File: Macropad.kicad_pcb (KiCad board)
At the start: 2 copper layers, 62 x 83 mm, 21 parts, among them SW1 SW_Push, SW10 RotaryEncoder_Switch, SW2 SW_Push, SW3 SW_Push, SW4 SW_Push, SW5 SW_Push, SW6 SW_Push, SW7 SW_Push, SW8 SW_Push, SW9 SW_Push, U1 MOUDLE-SEEEDUINO-XIAO, U2 OLED_0.91_128x32

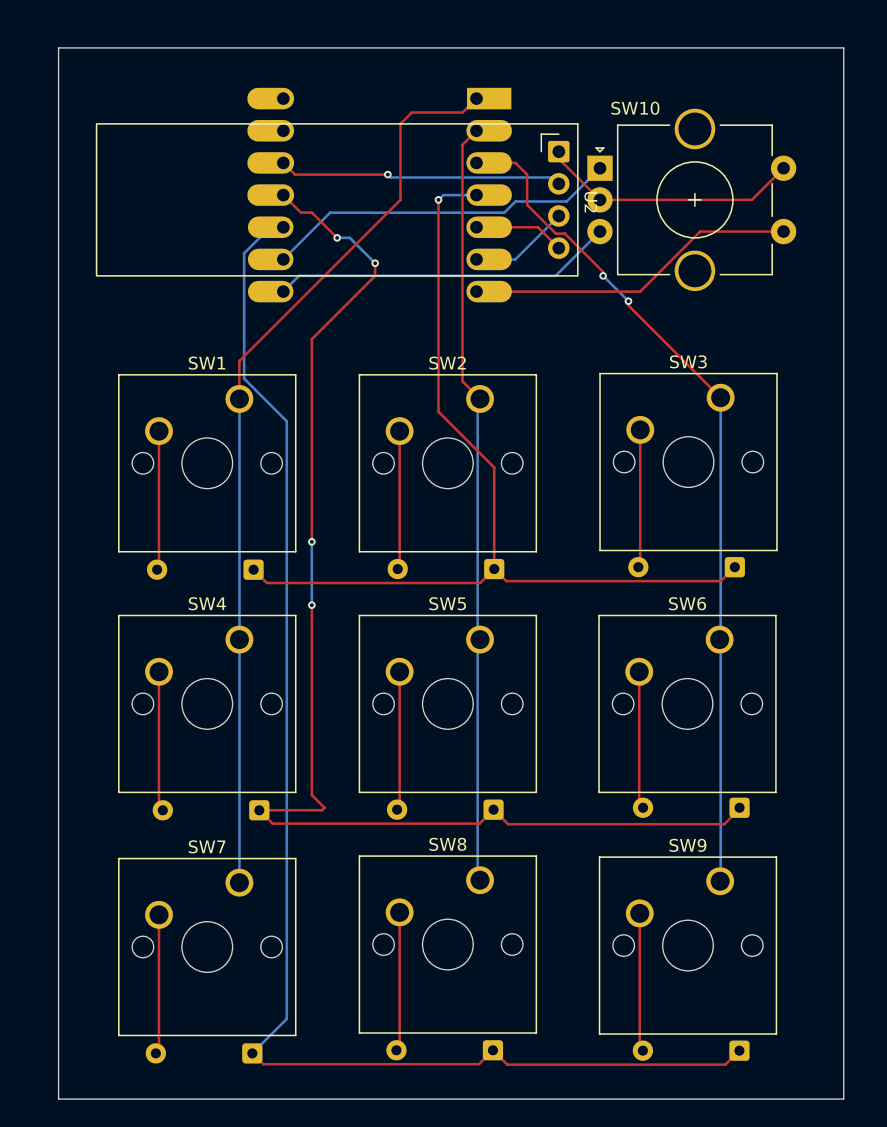
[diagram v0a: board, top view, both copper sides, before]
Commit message: noch löcher hinzugefügt
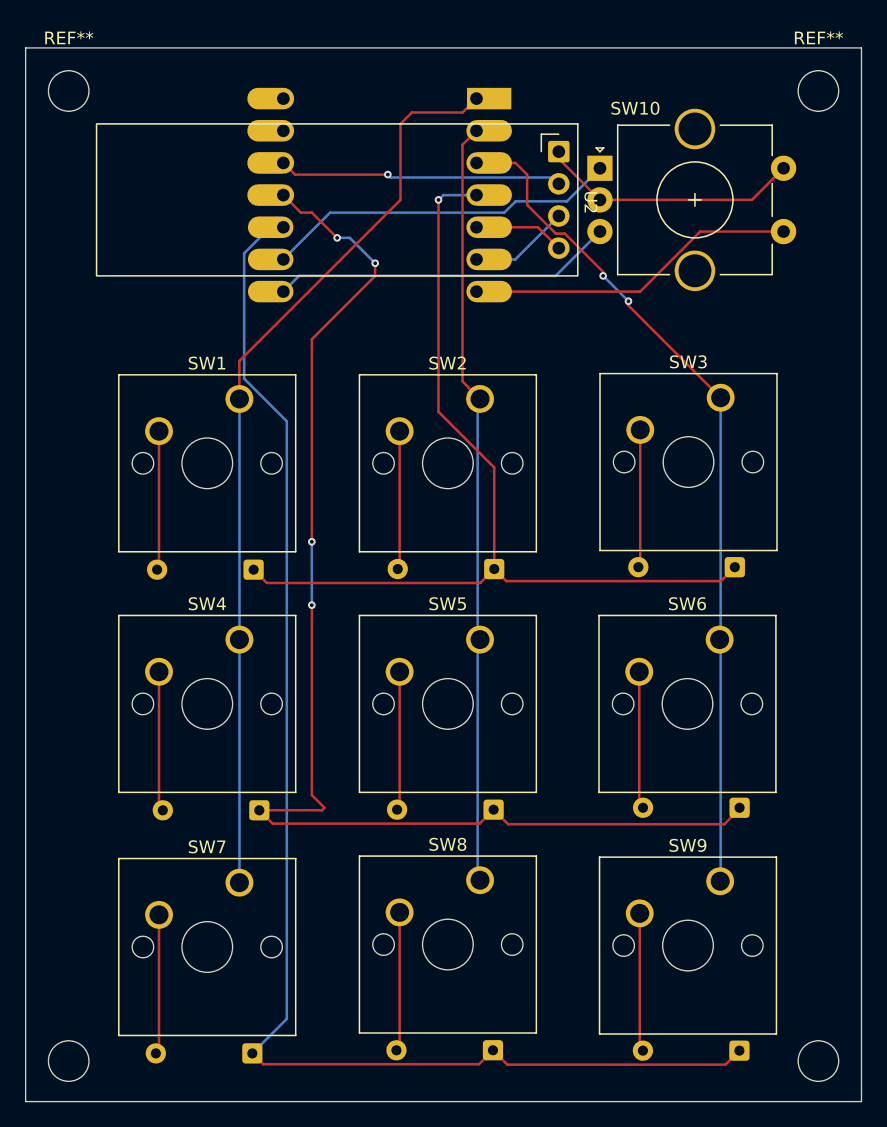
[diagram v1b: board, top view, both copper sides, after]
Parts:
- added REF**: MountingHole_3.2mm_M3, MountingHole:MountingHole_3.2mm_M3, F.Cu at (81.8, 56.4)
- added REF**: MountingHole_3.2mm_M3, MountingHole:MountingHole_3.2mm_M3, F.Cu at (141.0, 56.4)
- added REF**: MountingHole_3.2mm_M3, MountingHole:MountingHole_3.2mm_M3, F.Cu at (141.0, 133.0)
- added REF**: MountingHole_3.2mm_M3, MountingHole:MountingHole_3.2mm_M3, F.Cu at (81.8, 133.0)
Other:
- board size 62 x 83 mm -> 66 x 83.2 mm
